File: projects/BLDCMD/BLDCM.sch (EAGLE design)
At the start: 42 parts, among them IC1 STM32F103C8, IC3 NCV7351D1E, IC4 74AHCT1G08DCK, IC5 74AHCT1G08DCK, IC6 74AHCT1G08DCK, Q1 N-MOSFET-, Q2 N-MOSFET-, Q3 N-MOSFET-, Q4 N-MOSFET-, Q5 N-MOSFET-, Q6 N-MOSFET-, X1 8P8C-LED

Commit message: almost finish schematic
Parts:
- added C10, C14, C16: (no value), rcl:CPOL-EUE2.5-5
- added C11, C13: (no value), rcl:CPOL-EUE5-10.5
- added C12, C15, C9: 100n, mylib:C-EUC0603
- added C4, C5, C6, C7: 100n, rcl:C-EUC0603
- added C8: (no value), mylib:C-EUC0603
- added CN1: (no value), jst-xh:S6B-XH-A
- added D4: (no value), mylib:DIODE-SOD123
- added F1: (no value), mylib:R-EU_R1206
- added IC10: 7805DT, mylib:7824DT
- added IC7: SI8621AB-B-IS, mylib:SI8621AB-B-IS
- added IC8: 7815DT, mylib:7824DT
- added IC9: MC34063AD, mylib:MC34063AD
- added L1: L5852, mylib:L5852
- added R16, R17, R18: 1k, mylib:R-EU_R0603
- added R19, R20, R21: (no value), mylib:R-EU_R0603
- added U$2: TLP184, mylib:TLP184
- added U$3: XH-4-SIDE, con-xh:XH-4-SIDE
- added U$4: SWITCH_TACTILETOP, switch-tactile:SWITCH_TACTILETOP
- added U$6: XC6206, torex:XC6206
- added U$8: MA04-2, mylib:MA04-2
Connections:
- new net !RESET: C7.1, IC1.NRST, U$4.2
- new net +5V: C14.+, C9.1, CN1.2, L1.2, R19.2, U$3.2, U$6.VIN, U$8.5
- new net 24V_ISO: C15.1, C16.+, F1.1, IC10.VI
- new net 5V_ISO: IC10.VO, IC3.EN, IC3.VS, IC7.VDD2
- new net ENC_A: IC1.PA0-WKUP, U$3.3
- new net ENC_B: IC1.PA1, U$3.4
- new net GNDA: C10.-, C11.-, C12.2, C13.-, C14.-, C8.2, C9.2, D4.A, IC7.GND1, IC8.GND, IC9.GND, R20.1, U$6.VSS
- new net GNDIO: C15.2, C16.-, IC10.GND, IC3.GND, IC3.S, IC7.GND2, X1.3, X1.7, X1.8, X1.SHIELD
- new net IN_A: CN1.3, IC1.PA2
- new net IN_B: CN1.4, IC1.PA3
- new net IN_C: CN1.5, IC1.PB10
- new net IN_D: CN1.6, IC1.PB11
- new net ISENSE: IC1.PA4
- new net N$11: IC1.PA8, IC5A.I1, R17.2
- new net N$21: IC3.RXD, IC7.B2
- new net N$22: X1.6
- new net N$26: F1.2, X1.4, X1.5
- new net N$27: D4.C, IC9.SWE, L1.1
- new net N$28: IC9.FB, R19.1, R20.2
- new net N$29: IC9.DC, IC9.IS, IC9.SWC, R21.1
- new net N$30: C8.1, IC9.TC
- new net UART_RX: IC1.PB7, U$8.1
- new net UART_TX: IC1.PB6, U$8.3
- new net VSENSE: IC1.PA5
- net !EMS: now also U$2.AC2
- net +15V: now also C10.+, IC8.VO
- net +3V3: now also C12.1, C4.1, C5.1, C6.1, IC7.VDD1, U$2.AC1, U$6.VOUT, U$8.8
- net AGND: now also C4.2, C5.2, C6.2, C7.2, CN1.1, IC1.BOOT0, R16.1, R17.1, R18.1, U$3.1, U$4.1, U$8.2, U$8.7
- net CANRX: now also IC7.A2
- net CANTX: now also IC7.A1
- net LED0: now also IC1.PA6
- net LED1: now also IC1.PA7
- net LED2: now also IC1.PB0
- net LIN1: now also IC1.PB14; no longer IC1.PA6
- net LIN2: now also IC1.PB13; no longer IC1.PB7
- net LIN3: now also IC1.PA11; no longer IC1.PB6
- net N$3: now also IC1.PA9, R18.2; no longer IC1.PA7
- net N$4: now also IC3.TXD, IC7.B1; no longer IC1.PB0, IC5A.I1
- net N$5: now also IC1.PB15, R16.2; no longer IC1.PB1
- net SWCLK: now also U$8.4
- net SWDIO: now also U$8.6
- net VCC: now also C11.+, C13.+, IC8.VI, IC9.VCC, R21.2

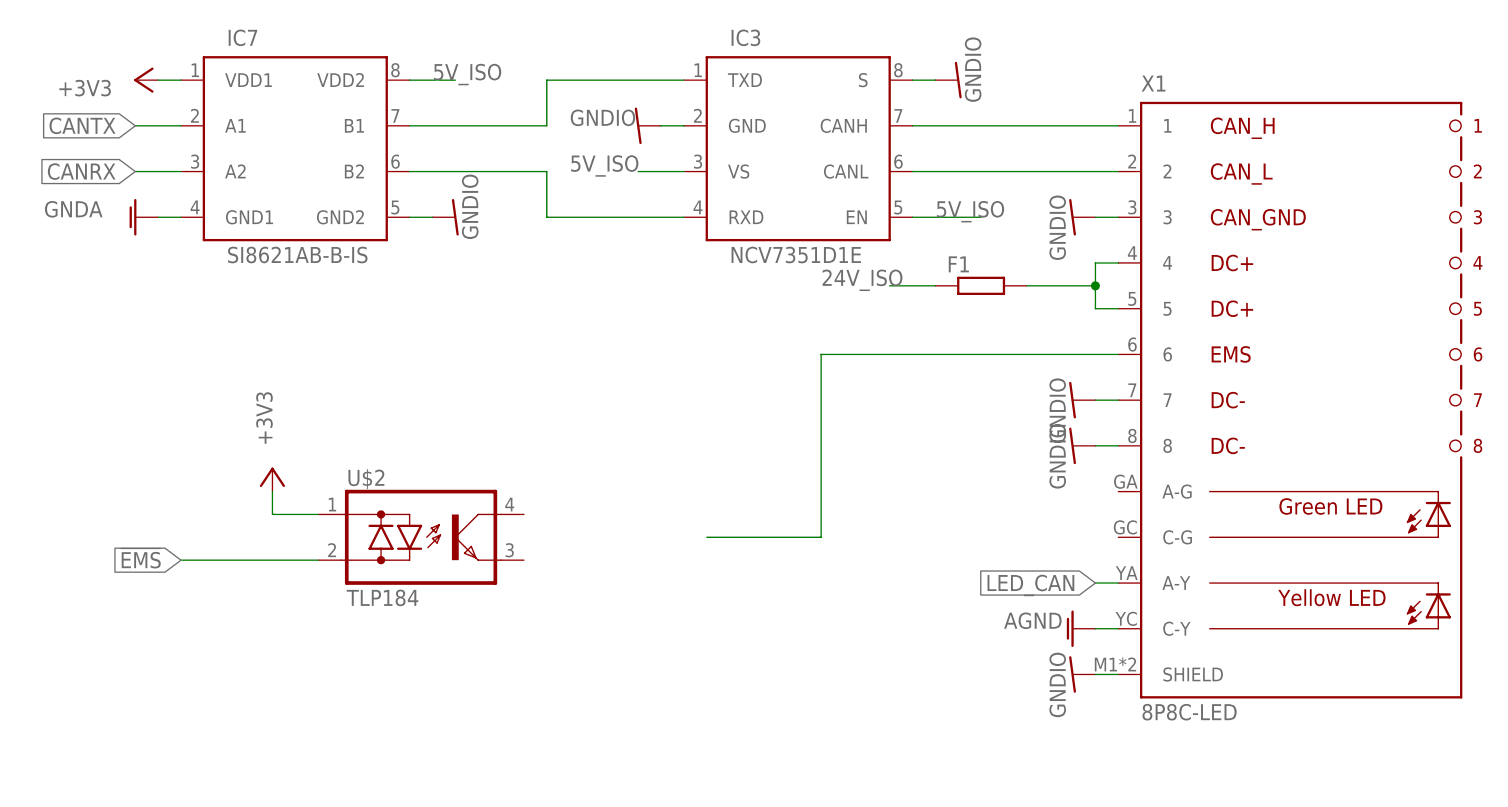
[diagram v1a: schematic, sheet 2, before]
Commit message: usbcan 修正済み　BLDCMD完成
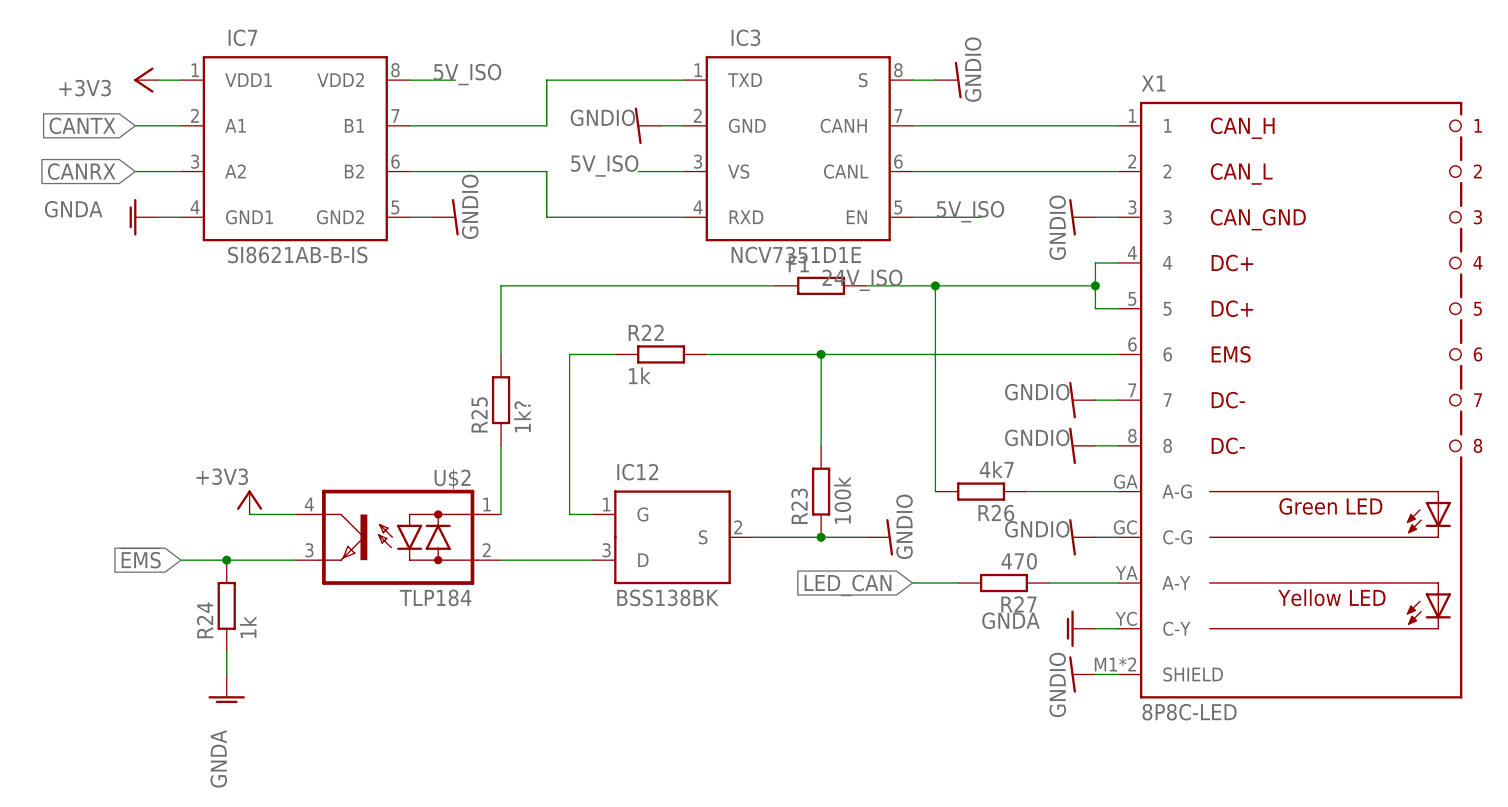
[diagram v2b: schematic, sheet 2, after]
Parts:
- added B1: FERRITE_BEAD, mylib:R-EU_R0603
- added C17, C18, C19: (no value), rcl:C-EUC0603
- added C20: 10u, rcl:C-EUC0603
- added C21: 1u, rcl:C-EUC0603
- added IC12: BSS138BK, mylib:BSS138BK
- added R22, R24: 1k, mylib:R-EU_R0603
- added R23: 100k, mylib:R-EU_R0603
- added R25: 1k?, mylib:R-EU_R0603
- added R26: 4k7, mylib:R-EU_R0603
- added R27: 470, mylib:R-EU_R0603
- added R28: CSS2H-2512, mylib:CSS2H-2512
- added R29, R30, R31: 10, mylib:R-EU_R0603
- added U$5: NCS199, mylib:NCS199
- X1: device con-rj45:8P8C-LED -> mylib:8P8C-LED
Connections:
- removed net AGND: C4.2, C5.2, C6.2, C7.2, CN1.1, IC1.BOOT0, IC1.VSS$1, IC1.VSS$2, IC1.VSS$3, IC2.GND, LED1.C, LED2.C, LED3.C, R16.1, R17.1, R18.1, U$1.2, U$3.1, U$4.1, U$8.2, U$8.7, X1.C-Y
- new net 3V3A: B1.1, C18.1, C20.1, C21.1, IC1.VDDA, U$5.VS
- new net N$31: IC12.G, R22.1
- new net N$32: IC12.D, U$2.AC2
- new net N$33: R25.1, U$2.AC1
- new net N$36: R26.1, X1.A-G
- new net N$37: R29.1, U$5.OUT
- new net N$38: R27.1, X1.A-Y
- net !EMS: now also R24.2, U$2.E; no longer U$2.AC2
- net +3V3: now also B1.2, U$2.C; no longer U$2.AC1
- net 24V_ISO: now also R25.2
- net GNDA: now also C17.2, C18.2, C19.2, C20.2, C21.2, C4.2, C5.2, C6.2, C7.2, CN1.1, IC1.BOOT0, IC1.VSS$1, IC1.VSS$2, IC1.VSS$3, IC1.VSSA, IC2.GND, LED1.C, LED2.C, LED3.C, R16.1, R17.1, R18.1, R24.1, R28.1, R31.1, U$1.2, U$3.1, U$4.1, U$5.GND, U$5.REF, U$8.2, U$8.7, X1.C-Y
- net GNDIO: now also IC12.S, R23.1, X1.C-G
- net ISENSE: now also C17.1, R29.2
- net LED_CAN: now also R27.2; no longer X1.A-Y
- net N$18: now also Q5.SOURCE, Q6.SOURCE, R10.2, R12.2, R28.2
- net N$19: now also R28.2S, U$5.IN+; no longer Q5.SOURCE, R10.2
- net N$20: now also R28.1S, U$5.IN-; no longer Q6.SOURCE, R12.2
- net N$22: now also R22.2, R23.2
- net N$26: now also R26.2
- net VCC: now also R30.2
- net VSENSE: now also C19.1, R30.1, R31.2
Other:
- moved on the sheet: F1, U$2, U$3
